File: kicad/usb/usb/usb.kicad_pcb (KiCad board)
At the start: 2 copper layers, 31 x 27 mm, 17 parts, among them J1 USB_C_Receptacle_USB2.0_14P, J2 PH2.0mm 2P, J3 Conn_01x07_Pin, SW1 PWR, U1 S-T111B33MC-OGSTFU, U2 MCP73831-2-OT

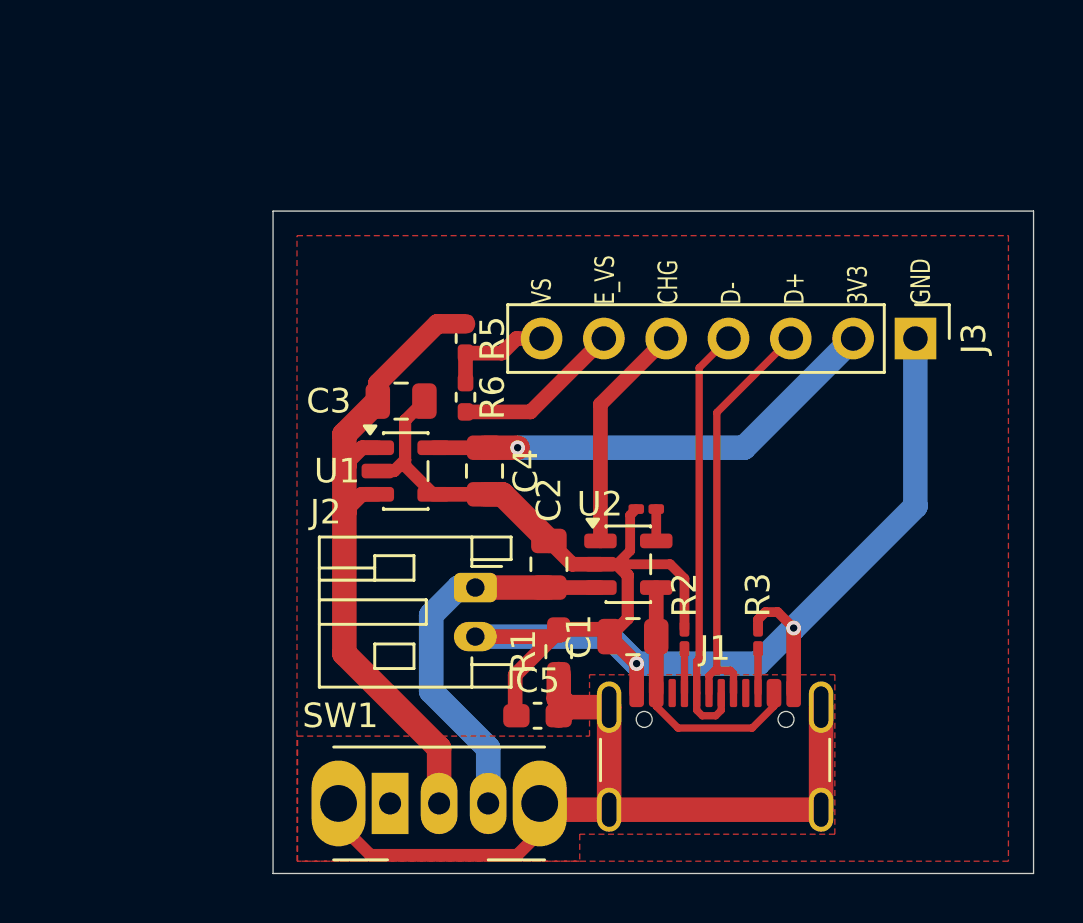
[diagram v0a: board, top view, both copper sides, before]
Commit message: Working on usb fabrication
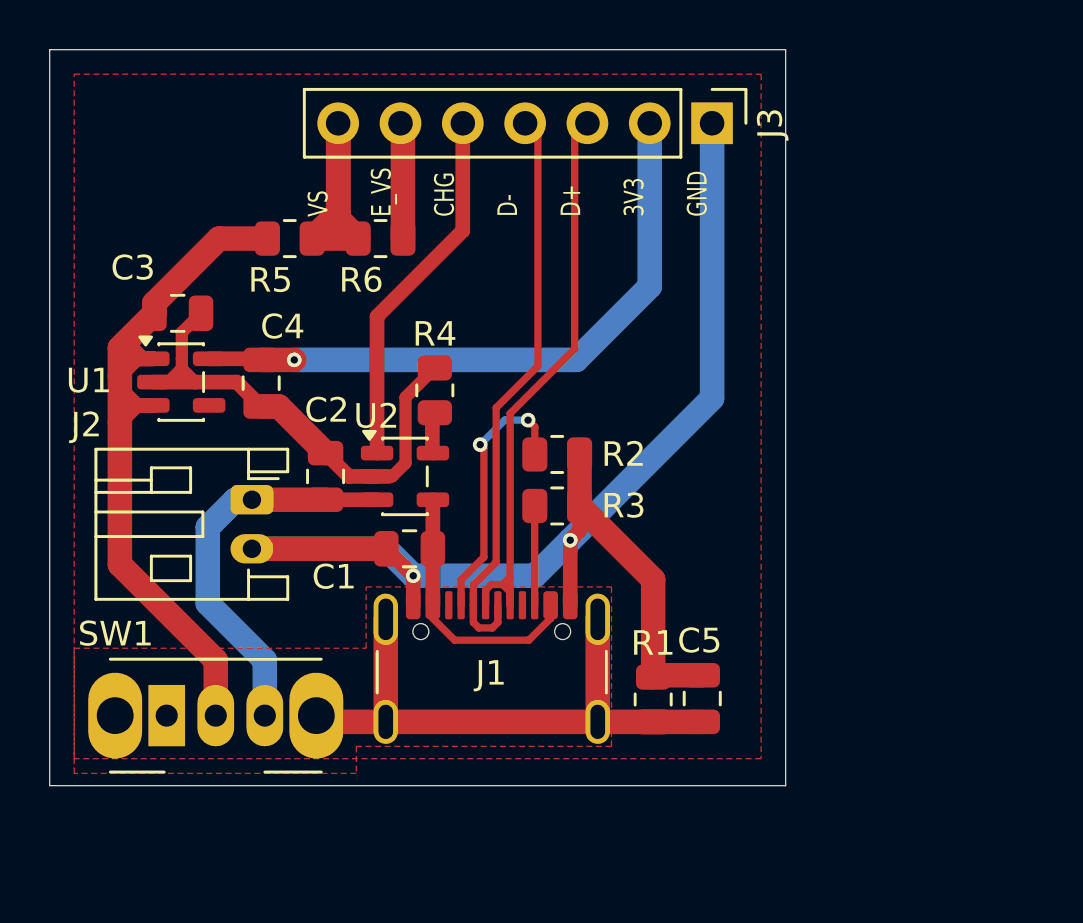
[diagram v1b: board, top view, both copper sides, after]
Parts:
- C5: footprint Capacitor_SMD:C_0603_1608Metric_Pad1.08x0.95mm_HandSolder -> Capacitor_SMD:C_0805_2012Metric
- R1: footprint Resistor_SMD:R_0603_1608Metric_Pad0.98x0.95mm_HandSolder -> Resistor_SMD:R_0805_2012Metric
- R2, R3, R4: footprint Resistor_SMD:R_0201_0603Metric_Pad0.64x0.40mm_HandSolder -> Resistor_SMD:R_0805_2012Metric
- R5, R6: footprint Resistor_SMD:R_0402_1005Metric_Pad0.72x0.64mm_HandSolder -> Resistor_SMD:R_0805_2012Metric
- U1: value S-T111B33MC-OGSTFU -> AP2112K-3.3
- moved J3 12.1 mm to (97.0, 83.0)
- moved R4 9.88 mm to (85.7, 93.9), turned to -90 degrees
- moved U1 9.84 mm to (75.4, 93.5)
- moved R3 9.82 mm to (90.7, 98.6), turned to 0 degrees
- moved C1 9.78 mm to (84.7, 100.3)
- moved C3 9.78 mm to (75.2, 90.7)
- moved J1 9.78 mm to (88.0, 106.3)
- moved SW1 9.78 mm to (74.8, 107.1)
- moved U2 9.78 mm to (84.5, 97.4)
- moved C2 9.78 mm to (81.2, 97.4)
- moved C4 9.78 mm to (78.6, 93.6)
- moved J2 9.78 mm to (78.2, 98.3)
- moved R2 9.13 mm to (90.7, 96.5), turned to 0 degrees
- moved R5 8.24 mm to (79.8, 87.7), turned to 180 degrees
- moved R6 7.34 mm to (83.5, 87.7), turned to 180 degrees
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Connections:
- net Net-(U2-V_{DD}) renamed USB5V
- SW1 pad : (no net) -> SHIELD
- U1 pad 4: GND -> unconnected-(U1-NC-Pad4)
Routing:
- net SHIELD: track 34.7 -> 24.2 mm
- net Net-(J1-CC1): track 1.80 -> 10.9 mm, vias 0 -> 2
- net GND: track 71.4 -> 79.0 mm
- net READ_VSENSE: track 4.55 -> 12.1 mm
- net +3V3: track 18.9 -> 25.9 mm
- net USB_D+: track 18.1 -> 24.2 mm
- net USB_D-: track 17.6 -> 23.5 mm
- net VSENSE: track 27.2 -> 33.1 mm
- net CHG: track 9.36 -> 14.9 mm
- net Net-(J1-CC2): track 1.80 -> 4.05 mm
- net EN_VSENSE: track 6.88 -> 4.74 mm
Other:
- board size 31 x 27 mm -> 30 x 30 mm

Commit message: Ordered USB board
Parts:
- removed the C5 at (96.6, 106.5)
- removed the R1 at (94.6, 106.5)
- added C3: 1u, Capacitor_SMD:C_0805_2012Metric, F.Cu at (77.9, 85.5)
- added U3: HX809T-3.08V, Package_TO_SOT_SMD:SOT-23, F.Cu at (77.8, 88.4)
- U2: renamed from U1; value AP2112K-3.3 -> LW5233A23E
- moved C5 6.35 mm to (72.5, 91.9), turned to 90 degrees
- moved C4 4.06 mm to (75.9, 94.7), turned to 180 degrees
- moved R4 2.92 mm to (80.9, 90.4)
- moved R5 2.92 mm to (84.6, 90.4)
- moved U2 1.66 mm to (75.8, 91.9), turned to 180 degrees
- renumbered C3 to C4, C4 to C5, R2 to R1, R3 to R2, R4 to R3, R5 to R4, R6 to R5, U2 to U1
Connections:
- J1 pad S1: SHIELD -> GND
- SW1 pad : SHIELD -> (no net)
- U2 pad 3: VSENSE -> LDO_EN
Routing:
- net SHIELD: track 24.2 -> 0.00 mm
- net GND: track 79.0 -> 90.5 mm
- net VSENSE: track 33.1 -> 28.0 mm
- net +3V3: track 25.9 -> 30.1 mm
- net EN_VSENSE: track 4.74 -> 7.91 mm
- net READ_VSENSE: track 12.1 -> 9.30 mm
- net LDO_EN: track 0.00 -> 1.65 mm
- net CHG: track 14.9 -> 15.7 mm
- added copper zone on F.Cu, net VSENSE
- removed copper zone on F.Cu, net SHIELD

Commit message: Tons of changes regarding batteries...
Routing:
- net GND: track 90.5 -> 95.9 mm
